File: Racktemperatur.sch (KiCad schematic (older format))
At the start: 24 parts, among them J1 Conn_01x03, J2 Conn_01x03, J3 Barrel_Jack_MountingPin, J4 Screw_Terminal_01x02, Q1 IRLZ44N, U1 74HC595, U2 74HC595, U3 DS18B20, U4 L7805

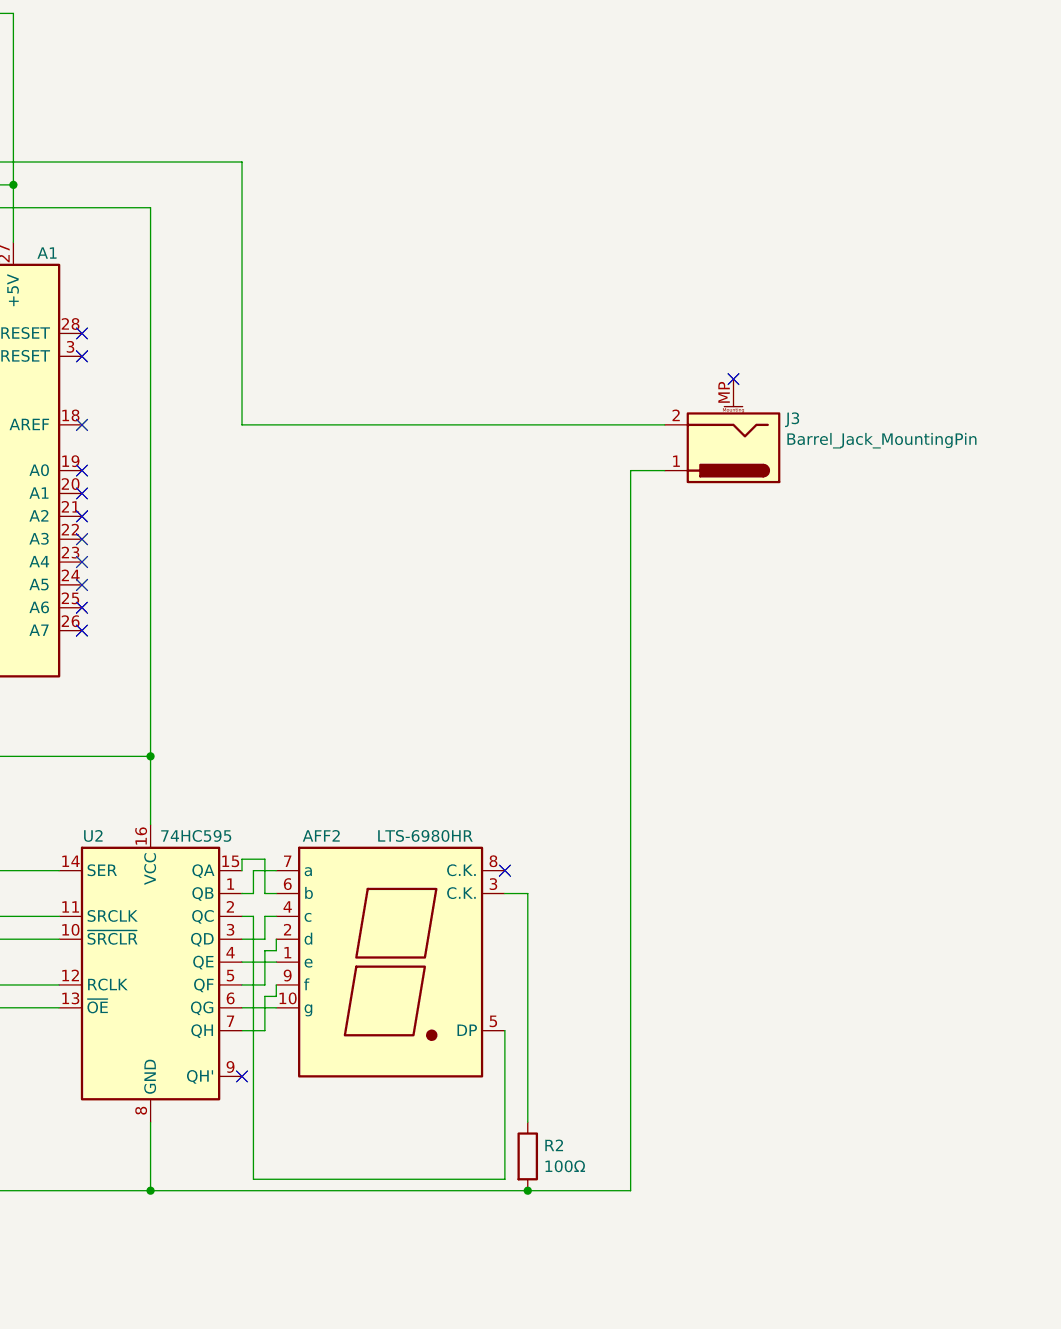
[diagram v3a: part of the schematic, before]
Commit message: Changed polarity of barrel jack
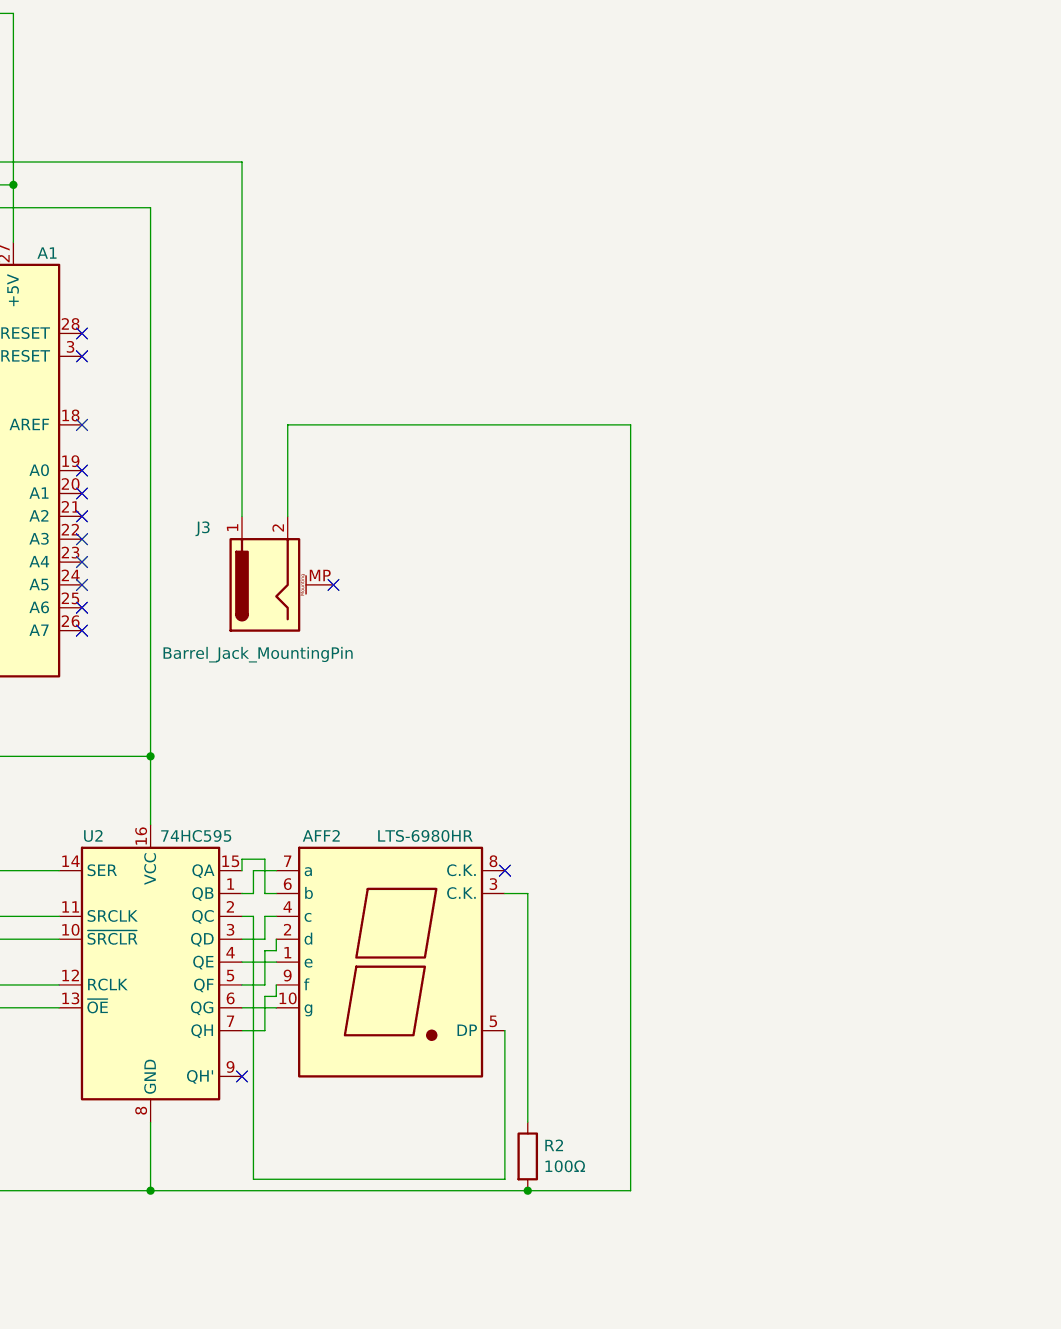
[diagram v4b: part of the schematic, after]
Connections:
- net +12V: now also J3.1; no longer J3.2
- net GND: now also J3.2; no longer J3.1
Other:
- moved on the sheet: J3
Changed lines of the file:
@@
 Sheet 1 1
 Title "Rack Temperature Control"
-Date "2019-10-26"
+Date "2019-11-12"
 Rev "1.5"
 Comp "haus-automatisierung.com"
@@
 Wire Wire Line
 	4600 3250 4450 3250
-$Comp
-L Connector:Barrel_Jack_MountingPin J3
-U 1 1 5CA80C86
-P 9000 3000
-F 0 "J3" H 8771 2873 50  0000 R CNN
-F 1 "Barrel_Jack_MountingPin" H 8771 2964 50  0000 R CNN
-F 2 "Connector_BarrelJack:BarrelJack_Wuerth_6941xx301002" H 9050 2960 50  0001 C CNN
-F 3 "~" H 9050 2960 50  0001 C CNN
-	1    9000 3000
-	-1   0    0    1
-$EndComp
-Wire Wire Line
-	8700 2900 6850 2900
-Wire Wire Line
-	6850 2900 6850 1750
-Wire Wire Line
-	8700 3100 8550 3100
-Wire Wire Line
-	8550 3100 8550 6250
 Wire Wire Line
 	8550 6250 8100 6250
@@
 NoConn ~ 8000 4850
 NoConn ~ 5350 4900
-NoConn ~ 9000 2700
+NoConn ~ 7250 3600
 Wire Wire Line
 	4600 3100 4450 3100
@@
 Wire Wire Line
 	4100 1500 4600 1500
+Wire Wire Line
+	8550 2900 8550 6250
+$Comp
+L Connector:Barrel_Jack_MountingPin J3
+U 1 1 5CA80C86
+P 6950 3600
+F 0 "J3" V 7200 3900 50  0000 R CNN
+F 1 "Barrel_Jack_MountingPin" V 6650 4050 50  0000 R CNN
+F 2 "Connector_BarrelJack:BarrelJack_Wuerth_6941xx301002" H 7000 3560 50  0001 C CNN
+F 3 "~" H 7000 3560 50  0001 C CNN
+	1    6950 3600
+	0    -1   -1   0
+$EndComp
+Wire Wire Line
+	6850 1750 6850 3300
+Wire Wire Line
+	7050 3300 7050 2900
+Wire Wire Line
+	7050 2900 8550 2900
 $EndSCHEMATC
